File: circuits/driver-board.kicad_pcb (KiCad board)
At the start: 4 copper layers, 40 x 47 mm, 74 parts, among them J1 Conn_01x18_Female, J2 USB4120-03-C_REVA, J3 Motor_Conn_01x04, J4 Screw_Terminals, J5 Conn_01x06_Female, Q1 SS8050-G, Q2 SS8050-G, SW1 RST_SW_Push, U1 CP2102N-Axx-xQFN24, U2 BA33DD0T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

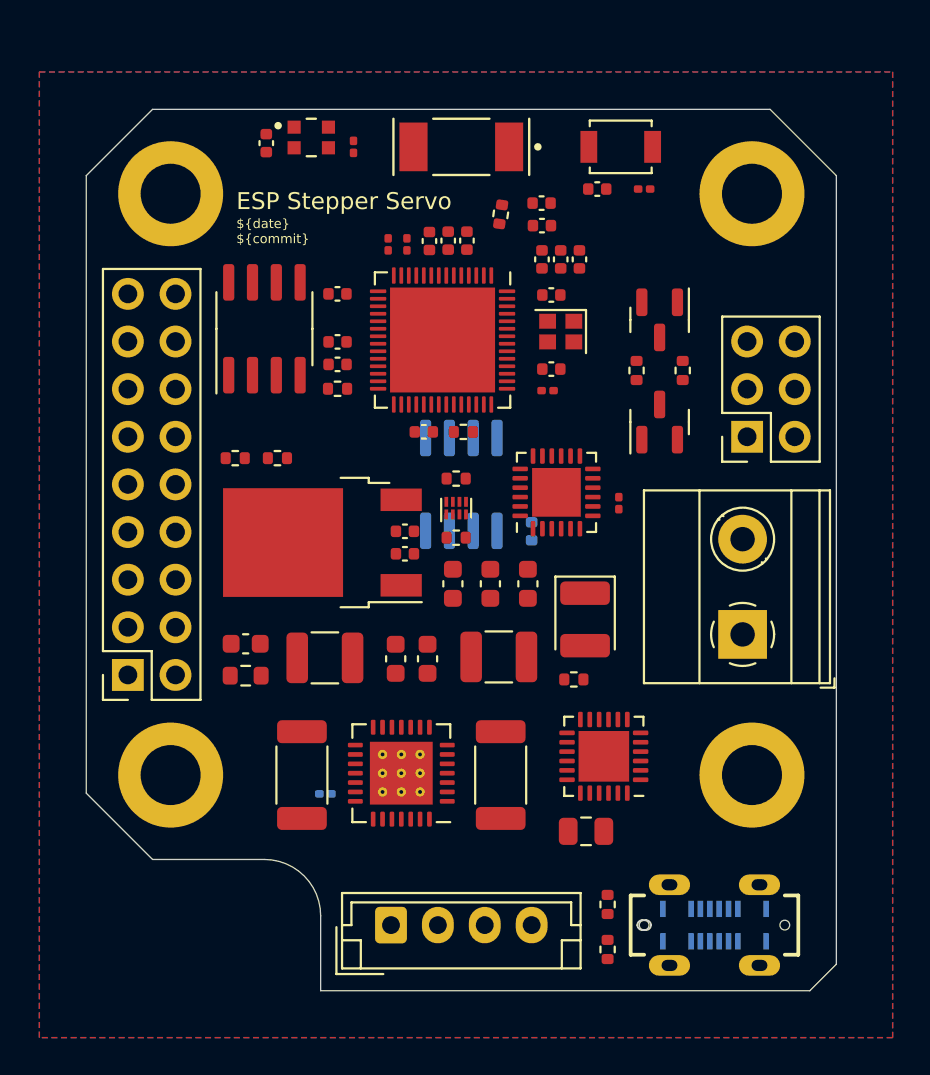
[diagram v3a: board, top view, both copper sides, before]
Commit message: another round of overall placement
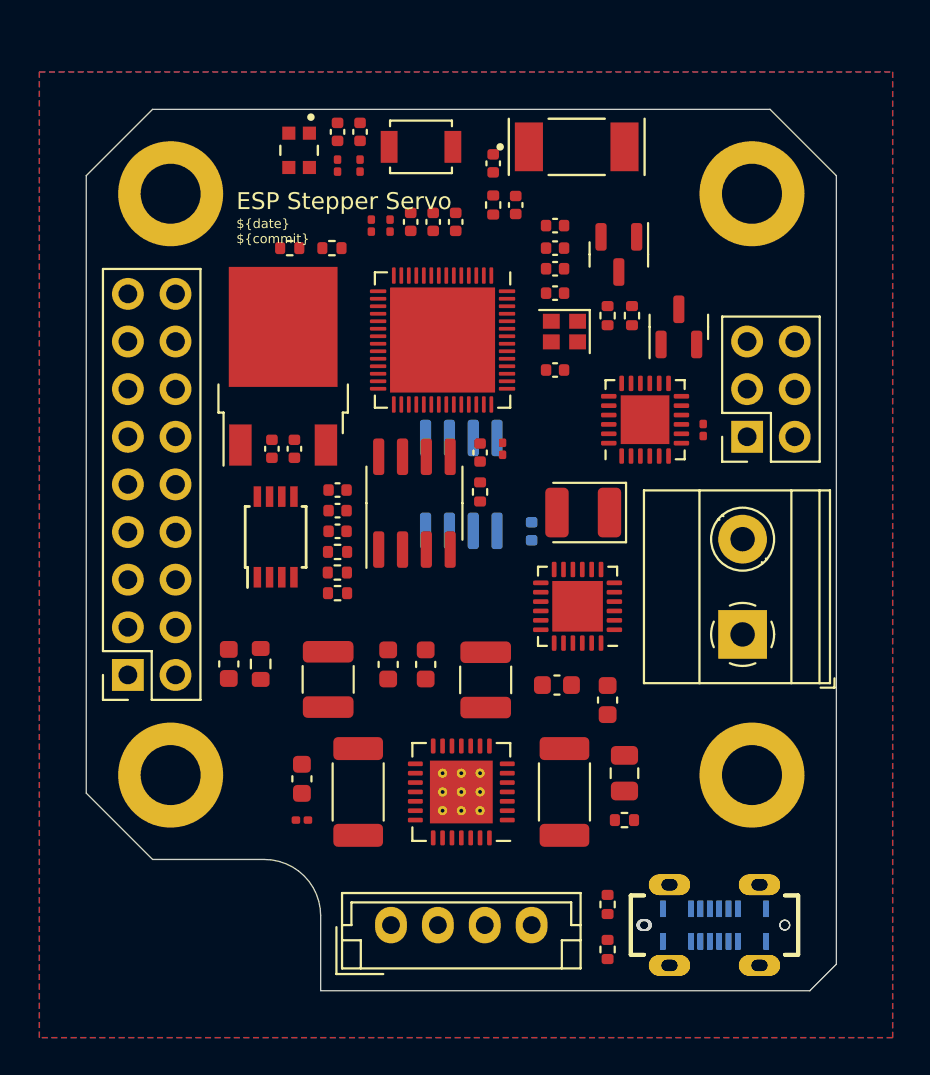
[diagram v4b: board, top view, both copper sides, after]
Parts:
- removed U: ESP-PSRAM32, Package_SO:SOIC-8_3.9x4.9mm_P1.27mm
- added J2: USB4120-03-C_REVA, Slimc_Connector_USB:GCT_USB4120-03-C_REVA, B.Cu at (63.5, 73.5)
- added U7: ESP-PSRAM32, Package_SO:SOIC-8_3.9x4.9mm_P1.27mm, F.Cu at (47.5, 51.0)
- R19: moved to F.Cu
- U8: footprint Package_SON:X2SON-8_1.4x1mm_P0.35mm -> Package_SO:TSSOP-8_3x3mm_P0.65mm
- moved C14 15.9 mm to (41.5, 65.7), turned to -90 degrees
- moved R1 15.2 mm to (44.6, 33.0), turned to 90 degrees
- moved C2 13.0 mm to (44.6, 31.2), turned to 90 degrees
- moved R6 12.3 mm to (43.1, 37.4), turned to 0 degrees
- moved R5 11.2 mm to (40.9, 37.4), turned to 0 degrees
- moved SW1 10.6 mm to (47.9, 32.0)
- moved C33 10.5 mm to (43.4, 50.3)
- moved U8 9.75 mm to (40.1, 52.8)
- moved U2 9.63 mm to (40.5, 43.7), turned to 90 degrees
- moved C3 9.04 mm to (39.9, 48.1), turned to 90 degrees
- moved C29 9.00 mm to (43.4, 51.4)
- moved C28 8.90 mm to (43.4, 52.5)
- moved C10 8.80 mm to (57.8, 61.5)
- moved R18 8.79 mm to (43.4, 55.8)
- moved R9 8.70 mm to (43.4, 53.6)
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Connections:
- J1 pad 10: /ESP_IO18 -> unconnected-(J1-Pad10)
- J1 pad 11: /ESP_IO17 -> unconnected-(J1-Pad11)
- J1 pad 12: /ESP_IO14 -> unconnected-(J1-Pad12)
- J1 pad 7: /ESP_IO03 -> unconnected-(J1-Pad7)
- J1 pad 8: /ESP_IO02 -> unconnected-(J1-Pad8)
- J1 pad 9: /USB_D- / ESP_IO19 -> unconnected-(J1-Pad9)
- J5 pad 3: /ESP_IO00 -> /ESP_EN
- J5 pad 4: /ESP_EN -> /UART0_TXD / ESP_IO43
- J5 pad 5: /UART0_RXD / ESP_IO44 -> /ESP_IO00
- J5 pad 6: /UART0_TXD / ESP_IO43 -> /UART0_RXD / ESP_IO44
- U3 pad 14: /ESP_IO09 -> /SR_Q / ESP_IO09
- U3 pad 15: /ESP_IO10 -> /SR_S / ESP_IO10
- U3 pad 41: unconnected-(U3-Pad41) -> /UART1_TXD / ESP_IO45
- U3 pad 42: unconnected-(U3-Pad42) -> /UART1_RXD / ESP_IO46
- U3 pad 51: /UART1_TXD / ESP_IO45 -> unconnected-(U3-Pad51)
- U3 pad 52: /UART1_RXD / ESP_IO46 -> unconnected-(U3-Pad52)
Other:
- rule pad_to_mask_clearance: 0 -> 0.0508

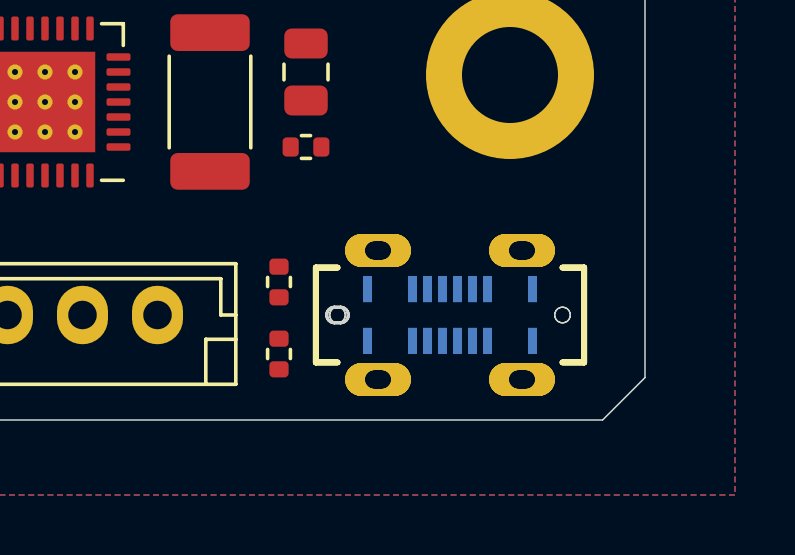
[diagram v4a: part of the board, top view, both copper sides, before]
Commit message: fixed duplicate usbc connector
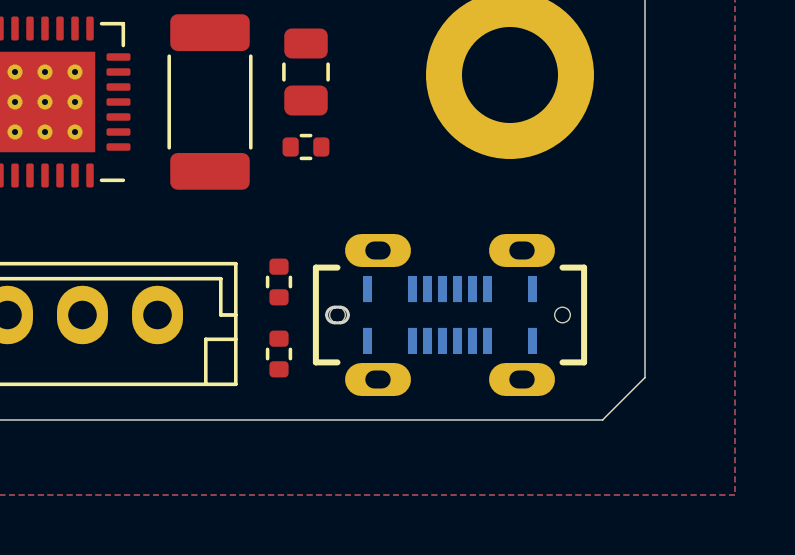
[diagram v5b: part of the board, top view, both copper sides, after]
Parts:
- removed the J2 at (63.5, 73.5)
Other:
- rule pad_to_mask_clearance: 0.0508 -> 0
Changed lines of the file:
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@@
       (dielectric_constraints no)
     )
-    (pad_to_mask_clearance 0.0508)
-    (solder_mask_min_width 0.25)
+    (pad_to_mask_clearance 0)
     (pcbplotparams
       (layerselection 0x00010fc_ffffffff)
@@
     )
   )
-  (footprint "Slimc_Connector_USB:GCT_USB4120-03-C_REVA" locked (layer "B.Cu")
-    (at 63.5 73.5 180)
-    (property "MANUFACTURER" "GCT")
-    (property "MAXIMUM_PACKAGE_HEIGHT" "6.5mm")
-    (property "PARTREV" "A")
-    (property "STANDARD" "Manufacturer Recommendations")
-    (property "Sheetfile" "driver-board.kicad_sch")
-    (property "Sheetname" "")
-    (attr through_hole)
-    (fp_text reference "J2" (at -1.524 3.937) (layer "B.SilkS") hide
-      (effects (font (size 1 1) (thickness 0.15)) (justify mirror))
-    )
-    (fp_text value "USB4120-03-C_REVA" (at -1.74 -4.44) (layer "B.Fab")
-      (effects (font (size 1 1) (thickness 0.15)) (justify mirror))
-    )
-    (fp_line (start 3.75 1.58) (end 4.47 1.58) (layer "B.SilkS") (width 0.2))
-    (fp_line (start -4.47 -1.58) (end -3.75 -1.58) (layer "B.SilkS") (width 0.2))
-    (fp_line (start 4.47 1.58) (end 4.47 -1.58) (layer "B.SilkS") (width 0.2))
-    (fp_line (start 4.47 -1.58) (end 3.75 -1.58) (layer "B.SilkS") (width 0.2))
-    (fp_line (start -4.47 1.58) (end -4.47 -1.58) (layer "B.SilkS") (width 0.2))
-    (fp_line (start -3.75 1.58) (end -4.47 1.58) (layer "B.SilkS") (width 0.2))
-    (fp_circle (center -5 0.9) (end -4.9 0.9) (layer "B.SilkS") (width 0.2) (fill none))
-    (fp_line (start 3.75 1.58) (end 4.47 1.58) (layer "F.SilkS") (width 0.2))
-    (fp_line (start -4.47 -1.58) (end -3.75 -1.58) (layer "F.SilkS") (width 0.2))
-    (fp_line (start -3.75 1.58) (end -4.47 1.58) (layer "F.SilkS") (width 0.2))
-    (fp_line (start 4.47 1.58) (end 4.47 -1.58) (layer "F.SilkS") (width 0.2))
-    (fp_line (start 4.47 -1.58) (end 3.75 -1.58) (layer "F.SilkS") (width 0.2))
-    (fp_line (start -4.47 1.58) (end -4.47 -1.58) (layer "F.SilkS") (width 0.2))
-    (fp_line (start 3.65 0.26) (end 3.85 0.26) (layer "Edge.Cuts") (width 0.1))
-    (fp_line (start 3.85 -0.26) (end 3.65 -0.26) (layer "Edge.Cuts") (width 0.1))
-    (fp_arc (start 4.11 0) (mid 4.033848 0.183848) (end 3.85 0.26) (layer "Edge.Cuts") (width 0.1))
-    (fp_arc (start 3.65 0.26) (mid 3.466152 0.183848) (end 3.39 0) (layer "Edge.Cuts") (width 0.1))
-    (fp_arc (start 3.85 -0.26) (mid 4.033848 -0.183848) (end 4.11 0) (layer "Edge.Cuts") (width 0.1))
-    (fp_arc (start 3.39 0) (mid 3.466152 -0.183848) (end 3.65 -0.26) (layer "Edge.Cuts") (width 0.1))
-    (fp_line (start 4.72 2.95) (end 4.72 -2.95) (layer "B.CrtYd") (width 0.05))
-    (fp_line (start -4.72 2.95) (end 4.72 2.95) (layer "B.CrtYd") (width 0.05))
-    (fp_line (start 4.72 -2.95) (end -4.72 -2.95) (layer "B.CrtYd") (width 0.05))
-    (fp_line (start -4.72 -2.95) (end -4.72 2.95) (layer "B.CrtYd") (width 0.05))
-    (fp_line (start -4.47 -1.58) (end -4.47 1.58) (layer "B.Fab") (width 0.1))
-    (fp_line (start 4.47 -1.58) (end -4.47 -1.58) (layer "B.Fab") (width 0.1))
-    (fp_line (start -4.47 1.58) (end 4.47 1.58) (layer "B.Fab") (width 0.1))
-    (fp_line (start 4.47 1.58) (end 4.47 -1.58) (layer "B.Fab") (width 0.1))
-    (fp_circle (center -5 0.9) (end -4.9 0.9) (layer "B.Fab") (width 0.2) (fill none))
-    (pad "" np_thru_hole circle locked (at -3.75 0 180) (size 0.52 0.52) (drill 0.52) (layers *.Cu *.Mask))
-    (pad "" np_thru_hole circle locked (at 3.75 0 180) (size 0.52 0.52) (drill 0.52) (layers *.Cu *.Mask))
-    (pad "A1" smd rect locked (at -2.75 0.865 180) (size 0.3 0.87) (layers "B.Cu" "B.Paste" "B.Mask")
-      (net 1 "GND") (pinfunction "GND_A") (pintype "power_in"))
-    (pad "A4" smd rect locked (at -1.25 0.865 180) (size 0.3 0.87) (layers "B.Cu" "B.Paste" "B.Mask")
-      (net 3 "VBUS") (pinfunction "VBUS_A") (pintype "power_in"))
-    (pad "A5" smd rect locked (at -0.75 0.865 180) (size 0.3 0.87) (layers "B.Cu" "B.Paste" "B.Mask")
-      (net 29 "/USB_CC1") (pinfunction "CC1") (pintype "bidirectional"))
-    (pad "A6" smd rect locked (at -0.25 0.865 180) (size 0.3 0.87) (layers "B.Cu" "B.Paste" "B.Mask")
-      (net 30 "/USB_D+") (pinfunction "D1+") (pintype "bidirectional"))
-    (pad "A7" smd rect locked (at 0.25 0.865 180) (size 0.3 0.87) (layers "B.Cu" "B.Paste" "B.Mask")
-      (net 32 "/USB_D-") (pinfunction "D1-") (pintype "bidirectional"))
-    (pad "A8" smd rect locked (at 0.75 0.865 180) (size 0.3 0.87) (layers "B.Cu" "B.Paste" "B.Mask")
-      (net 17 "unconnected-(J2-PadA8)") (pinfunction "SBU1") (pintype "bidirectional+no_connect"))
-    (pad "A9" smd rect locked (at 1.25 0.865 180) (size 0.3 0.87) (layers "B.Cu" "B.Paste" "B.Mask")
-      (net 3 "VBUS") (pinfunction "VBUS_A") (pintype "power_in"))
-    (pad "A12" smd rect locked (at 2.75 0.865 180) (size 0.3 0.87) (layers "B.Cu" "B.Paste" "B.Mask")
-      (net 1 "GND") (pinfunction "GND_A") (pintype "power_in"))
-    (pad "B1" smd rect locked (at 2.75 -0.865 180) (size 0.3 0.87) (layers "B.Cu" "B.Paste" "B.Mask")
-      (net 1 "GND") (pinfunction "GND_B") (pintype "power_in"))
-    (pad "B4" smd rect locked (at 1.25 -0.865 180) (size 0.3 0.87) (layers "B.Cu" "B.Paste" "B.Mask")
-      (net 3 "VBUS") (pinfunction "VBUS_B") (pintype "power_in"))
-    (pad "B5" smd rect locked (at 0.75 -0.865 180) (size 0.3 0.87) (layers "B.Cu" "B.Paste" "B.Mask")
-      (net 34 "/USB_CC2") (pinfunction "CC2") (pintype "bidirectional"))
-    (pad "B6" smd rect locked (at 0.25 -0.865 180) (size 0.3 0.87) (layers "B.Cu" "B.Paste" "B.Mask")
-      (net 30 "/USB_D+") (pinfunction "D2+") (pintype "bidirectional"))
-    (pad "B7" smd rect locked (at -0.25 -0.865 180) (size 0.3 0.87) (layers "B.Cu" "B.Paste" "B.Mask")
-      (net 32 "/USB_D-") (pinfunction "D2-") (pintype "bidirectional"))
-    (pad "B8" smd rect locked (at -0.75 -0.865 180) (size 0.3 0.87) (layers "B.Cu" "B.Paste" "B.Mask")
-      (net 18 "unconnected-(J2-PadB8)") (pinfunction "SBU2") (pintype "bidirectional+no_connect"))
-    (pad "B9" smd rect locked (at -1.25 -0.865 180) (size 0.3 0.87) (layers "B.Cu" "B.Paste" "B.Mask")
-      (net 3 "VBUS") (pinfunction "VBUS_B") (pintype "power_in"))
-    (pad "B12" smd rect locked (at -2.75 -0.865 180) (size 0.3 0.87) (layers "B.Cu" "B.Paste" "B.Mask")
-      (net 1 "GND") (pinfunction "GND_B") (pintype "power_in"))
-    (pad "S1" thru_hole oval locked (at -2.4 2.15 180) (size 2.2 1.1) (drill oval 0.85 0.6) (layers *.Cu *.Mask)
-      (net 1 "GND") (pinfunction "SHIELD") (pintype "passive"))
-    (pad "S2" thru_hole oval locked (at -2.4 -2.15 180) (size 2.2 1.1) (drill oval 0.85 0.6) (layers *.Cu *.Mask)
-      (net 1 "GND") (pinfunction "SHIELD") (pintype "passive"))
-    (pad "S3" thru_hole oval locked (at 2.4 2.15 180) (size 2.2 1.1) (drill oval 0.85 0.6) (layers *.Cu *.Mask)
-      (net 1 "GND") (pinfunction "SHIELD") (pintype "passive"))
-    (pad "S4" thru_hole oval locked (at 2.4 -2.15 180) (size 2.2 1.1) (drill oval 0.85 0.6) (layers *.Cu *.Mask)
-      (net 1 "GND") (pinfunction "SHIELD") (pintype "passive"))
-    (model "${SLIMC_3DMODELS}/GCT_USB412003C.models/USB4120-03-C.stp"
-      (offset (xyz 0 0 0))
-      (scale (xyz 1 1 1))
-      (rotate (xyz -90 0 0))
-    )
-  )

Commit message: first tracing
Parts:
- moved R7 17.1 mm to (51.0, 52.6), turned to 90 degrees
- moved R2 3.10 mm to (43.4, 51.6)
- moved R18 3.10 mm to (43.4, 52.7)
- moved R9 2.40 mm to (43.4, 56.0)
- moved C28 2.40 mm to (43.4, 54.9)
- moved C29 2.40 mm to (43.4, 53.8)
- moved U8 0.30 mm to (40.1, 53.1)
- moved C20 0.10 mm to (52.8, 35.1)
- moved R8 0.10 mm to (57.8, 72.3)
- moved AE1 0.10 mm to (56.1, 32.0)
- moved C34 0.10 mm to (51.6, 32.9)
- moved L1 0.10 mm to (51.6, 35.1)
- turned R6 to 180 degrees
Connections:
- J1 pad 15: /I2C_SDA / ESP_IO05 -> /I2C_SCL / ESP_IO04
- J1 pad 16: /I2C_SCL / ESP_IO04 -> /I2C_SDA / ESP_IO05
- R18 pad 1: /SR_S / ESP_IO10 -> /SR_S / ESP_IO21
- R2 pad 2: /SR_S / ESP_IO10 -> /SR_S / ESP_IO21
- U3 pad 12: /TMC2209_STEP / ESP_IO07 -> unconnected-(U3-Pad12)
- U3 pad 13: /TMC2209_DIR / ESP_IO08 -> unconnected-(U3-Pad13)
- U3 pad 14: /SR_Q / ESP_IO09 -> /ESP_IO09
- U3 pad 15: /SR_S / ESP_IO10 -> /ESP_IO10
- U3 pad 21: unconnected-(U3-Pad21) -> /TMC2209_STEP / ESP_IO15
- U3 pad 22: unconnected-(U3-Pad22) -> /TMC2209_DIR / ESP_IO16
- U3 pad 24: /ESP_IO18 -> /SR_Q / ESP_IO18
- U3 pad 27: /ESP_IO21 -> /SR_S / ESP_IO21
- U5 pad 16: /TMC2209_STEP / ESP_IO07 -> /TMC2209_STEP / ESP_IO15
- U5 pad 19: /TMC2209_DIR / ESP_IO08 -> /TMC2209_DIR / ESP_IO16
- U8 pad 5: /SR_Q / ESP_IO09 -> /SR_Q / ESP_IO18
- U8 pad 6: /SR_S / ESP_IO10 -> /SR_S / ESP_IO21
- U8 pad 7: /SR_Q / ESP_IO09 -> /SR_Q / ESP_IO18
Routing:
- net /TMC2209_EN / ESP_IO06: track 0.00 -> 56.1 mm, vias 0 -> 3
- net /UART1_RXD / ESP_IO46: track 0.00 -> 48.9 mm, vias 0 -> 2
- net /I2C_SCL / ESP_IO04: track 0.00 -> 34.0 mm, vias 0 -> 1
- net /USB_D+: track 0.00 -> 31.6 mm, vias 0 -> 1
- net /ESP_EN: track 0.00 -> 30.9 mm, vias 0 -> 2
- net /USB_D-: track 0.00 -> 30.9 mm, vias 0 -> 2
- net /I2C_SDA / ESP_IO05: track 0.00 -> 30.5 mm, vias 0 -> 1
- net /USB_CC1: track 0.00 -> 27.7 mm, vias 0 -> 3
- net /TMC2209_DIR / ESP_IO16: track 0.00 -> 27.2 mm, vias 0 -> 2
- net /TMC2209_STEP / ESP_IO15: track 0.00 -> 27.0 mm, vias 0 -> 2
- net /USB_CC2: track 0.00 -> 26.9 mm, vias 0 -> 3
- net /UART1_TXD / ESP_IO45: track 0.00 -> 24.9 mm, vias 0 -> 1
- net /ESP_IO00: track 0.00 -> 24.1 mm, vias 0 -> 2
- net +3V3: track 0.00 -> 22.1 mm
- net /UART0_RXD / ESP_IO44: track 0.00 -> 20.5 mm, vias 0 -> 1
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
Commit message: ore tracing
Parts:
- moved C33 12.7 mm to (54.6, 44.3), turned to 90 degrees
- moved C14 6.46 mm to (46.8, 62.0), turned to 0 degrees
- moved C26 0.89 mm to (55.8, 44.3), turned to 90 degrees
- moved R5 0.56 mm to (40.3, 37.4)
- turned C27 to 90 degrees
- turned C35 to 180 degrees
- turned R14 to -90 degrees
- turned R7 to -90 degrees
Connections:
- H1 pad 1: (no net) -> GND
- H2 pad 1: (no net) -> GND
- H3 pad 1: (no net) -> GND
- H4 pad 1: (no net) -> GND
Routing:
- net +3V3: track 22.1 -> 84.4 mm, vias 0 -> 30
- net VBUS: track 11.1 -> 60.8 mm, vias 0 -> 51
- net Net-(R12-Pad2): track 0.00 -> 8.70 mm
- net Net-(R13-Pad2): track 0.00 -> 8.66 mm
- net Net-(C10-Pad2): track 0.00 -> 7.89 mm
- net /TMC2209_OB2: track 0.00 -> 6.14 mm, vias 0 -> 1
- net /TMC2209_OA2: track 0.00 -> 6.14 mm, vias 0 -> 1
- net GND: track 0.00 -> 5.45 mm, vias 0 -> 17
- net /ESP_IO47: track 1.11 -> 6.27 mm
- net /TMC2209_OB1: track 0.00 -> 4.96 mm
- net /TMC2209_OA1: track 0.00 -> 4.96 mm
- net /UART0_RXD / ESP_IO44: track 20.5 -> 18.6 mm, vias 1 -> 2
- net /UART0_TXD / ESP_IO43: track 19.7 -> 17.9 mm, vias 1 -> 2
- net /TMC2209_EN / ESP_IO06: track 56.1 -> 55.3 mm
- net /ESP_IO14: track 8.09 -> 8.65 mm
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- added copper zone on F.Cu, net +3V3
- added copper zone on F.Cu, net VBUS
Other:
- board text removed: "by Christian Skjerning"
